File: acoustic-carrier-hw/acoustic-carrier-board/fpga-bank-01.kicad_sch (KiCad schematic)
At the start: 8 parts, among them IC1 ECP5-BGA256

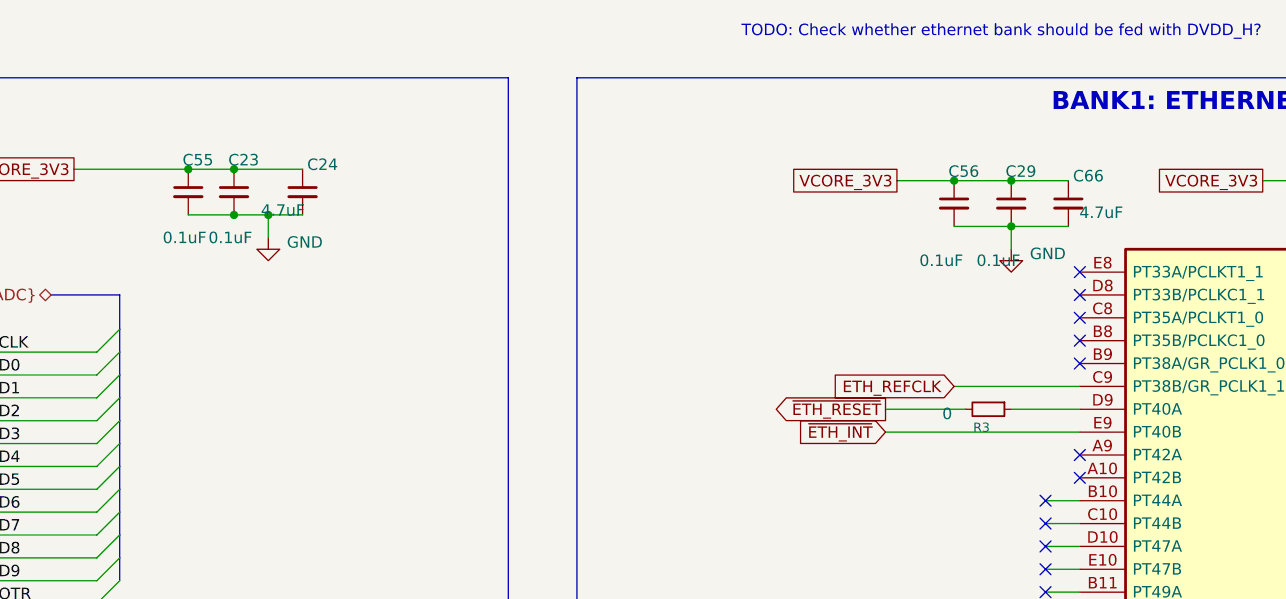
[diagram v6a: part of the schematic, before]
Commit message: [carrier] Finished rough layout, p (put together according to component category
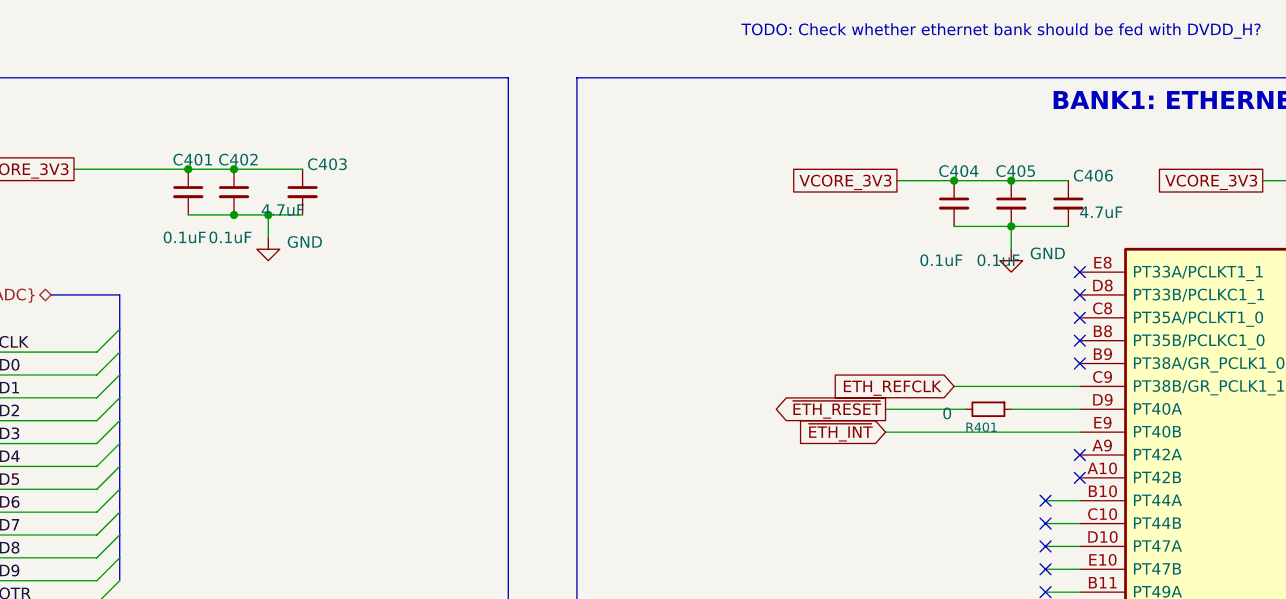
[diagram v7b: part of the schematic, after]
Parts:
- renumbered C55 to C401, C23 to C402, C24 to C403, C56 to C404, C29 to C405, C66 to C406, R3 to R401
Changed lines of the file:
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@@
 		(on_board yes)
 		(dnp no)
-		(property "Reference" "C55"
+		(property "Reference" "C401"
 			(at 115.824 45.974 0)
 			(effects
@@
 			(project "acoustic-carrier-board"
 				(path "/25b015c9-ab13-4427-b72c-b6f348597100/7e06bbd5-1e52-404d-be87-b09140719274"
-					(reference "C55")
+					(reference "C401")
 					(unit 1)
 				)
@@
 		(on_board yes)
 		(dnp no)
-		(property "Reference" "C66"
+		(property "Reference" "C406"
 			(at 211.328 47.752 0)
 			(effects
@@
 			(project "acoustic-carrier-board"
 				(path "/25b015c9-ab13-4427-b72c-b6f348597100/7e06bbd5-1e52-404d-be87-b09140719274"
-					(reference "C66")
+					(reference "C406")
 					(unit 1)
 				)
@@
 		(on_board yes)
 		(dnp no)
-		(property "Reference" "#PWR014"
+		(property "Reference" "#PWR0401"
 			(at 121.92 60.96 0)
 			(effects
@@
 			(project "acoustic-carrier-board"
 				(path "/25b015c9-ab13-4427-b72c-b6f348597100/7e06bbd5-1e52-404d-be87-b09140719274"
-					(reference "#PWR014")
+					(reference "#PWR0401")
 					(unit 1)
 				)
@@
 		(on_board yes)
 		(dnp no)
-		(property "Reference" "#PWR08"
+		(property "Reference" "#PWR0402"
 			(at 204.47 62.23 0)
 			(effects
@@
 			(project "acoustic-carrier-board"
 				(path "/25b015c9-ab13-4427-b72c-b6f348597100/7e06bbd5-1e52-404d-be87-b09140719274"
-					(reference "#PWR08")
+					(reference "#PWR0402")
 					(unit 1)
 				)
@@
 		(on_board yes)
 		(dnp no)
-		(property "Reference" "C56"
+		(property "Reference" "C404"
 			(at 200.914 47.244 0)
 			(effects
@@
 			(project "acoustic-carrier-board"
 				(path "/25b015c9-ab13-4427-b72c-b6f348597100/7e06bbd5-1e52-404d-be87-b09140719274"
-					(reference "C56")
+					(reference "C404")
 					(unit 1)
 				)
@@
 		(on_board yes)
 		(dnp no)
-		(property "Reference" "C24"
+		(property "Reference" "C403"
 			(at 126.238 46.482 0)
 			(effects
@@
 			(project "acoustic-carrier-board"
 				(path "/25b015c9-ab13-4427-b72c-b6f348597100/7e06bbd5-1e52-404d-be87-b09140719274"
-					(reference "C24")
+					(reference "C403")
 					(unit 1)
 				)
@@
 		(on_board yes)
 		(dnp no)
-		(property "Reference" "C23"
+		(property "Reference" "C402"
 			(at 120.904 45.974 0)
 			(effects
@@
 			(project "acoustic-carrier-board"
 				(path "/25b015c9-ab13-4427-b72c-b6f348597100/7e06bbd5-1e52-404d-be87-b09140719274"
-					(reference "C23")
+					(reference "C402")
 					(unit 1)
 				)
@@
 		(on_board yes)
 		(dnp no)
-		(property "Reference" "C29"
+		(property "Reference" "C405"
 			(at 207.264 47.244 0)
 			(effects
@@
 			(project "acoustic-carrier-board"
 				(path "/25b015c9-ab13-4427-b72c-b6f348597100/7e06bbd5-1e52-404d-be87-b09140719274"
-					(reference "C29")
+					(reference "C405")
 					(unit 1)
 				)
@@
 		(on_board yes)
 		(dnp no)
-		(property "Reference" "R3"
+		(property "Reference" "R401"
 			(at 201.168 75.692 90)
 			(effects
@@
 			(project "acoustic-carrier-board"
 				(path "/25b015c9-ab13-4427-b72c-b6f348597100/7e06bbd5-1e52-404d-be87-b09140719274"
-					(reference "R3")
+					(reference "R401")
 					(unit 1)
 				)

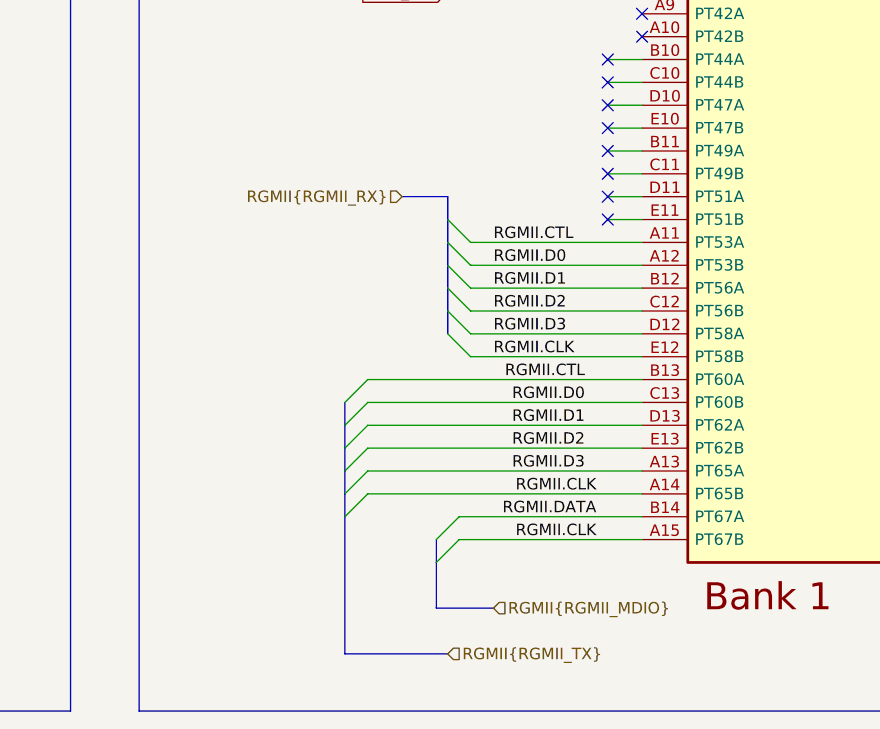
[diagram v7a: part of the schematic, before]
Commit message: [¢arrier] Added netties and determined trace geometry for 50 ohms SE / 100 ohms DIFF impedance (next) reset the appropriate DQS group signals, RGMII and USB signals
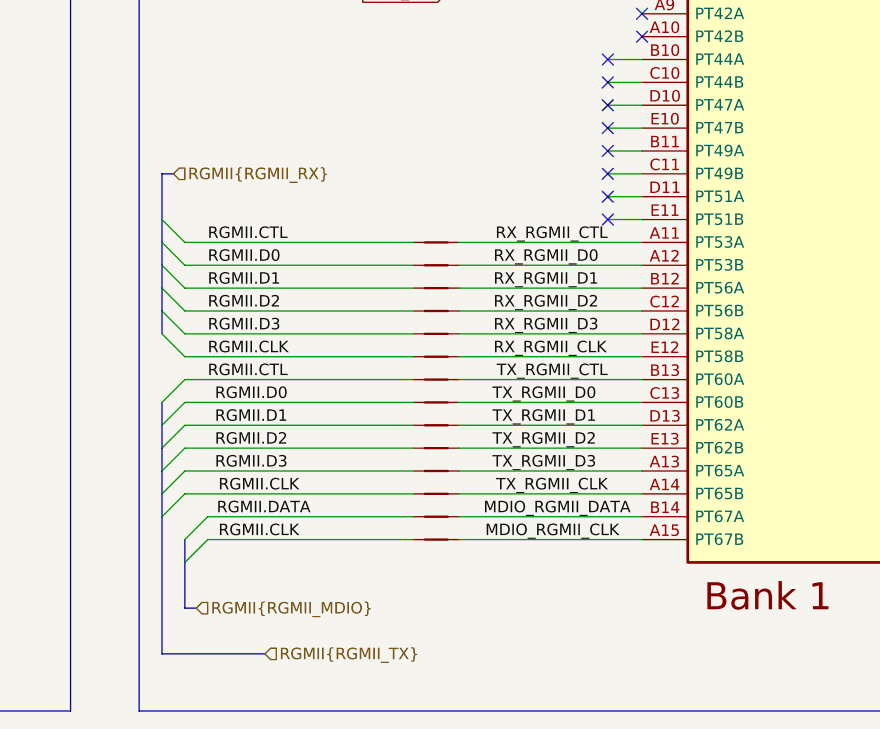
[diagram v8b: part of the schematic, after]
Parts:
- added NT401, NT402, NT403, NT404, NT405, NT406, NT407, NT408, NT409, NT410, NT415, NT416, NT417, NT418: NetTie_2, iw-misc:NetTie-2_SMD_Pad0.1565mm, symbol Device:NetTie_2
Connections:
- net RGMII.CLK: now also NT402.1, NT408.1, NT410.1; no longer IC1.A14 (PT65B), IC1.A15 (PT67B), IC1.E12 (PT58B)
- net RGMII.CTL: now also NT403.1, NT415.1; no longer IC1.A11 (PT53A), IC1.B13 (PT60A)
- net RGMII.D0: now also NT404.1, NT416.1; no longer IC1.A12 (PT53B), IC1.C13 (PT60B)
- net RGMII.D1: now also NT405.1, NT417.1; no longer IC1.B12 (PT56A), IC1.D13 (PT62A)
- net RGMII.D2: now also NT406.1, NT418.1; no longer IC1.C12 (PT56B), IC1.E13 (PT62B)
- net RGMII.D3: now also NT401.1, NT407.1; no longer IC1.A13 (PT65A), IC1.D12 (PT58A)
- net RGMII.DATA: now also NT409.1; no longer IC1.B14 (PT67A)
- new net MDIO_RGMII_CLK: IC1.A15 (PT67B), NT410.2
- new net MDIO_RGMII_DATA: IC1.B14 (PT67A), NT409.2
- new net RX_RGMII_CLK: IC1.E12 (PT58B), NT402.2
- new net RX_RGMII_CTL: IC1.A11 (PT53A), NT415.2
- new net RX_RGMII_D0: IC1.A12 (PT53B), NT416.2
- new net RX_RGMII_D1: IC1.B12 (PT56A), NT417.2
- new net RX_RGMII_D2: IC1.C12 (PT56B), NT418.2
- new net RX_RGMII_D3: IC1.D12 (PT58A), NT401.2
- new net TX_RGMII_CLK: IC1.A14 (PT65B), NT408.2
- new net TX_RGMII_CTL: IC1.B13 (PT60A), NT403.2
- new net TX_RGMII_D0: IC1.C13 (PT60B), NT404.2
- new net TX_RGMII_D1: IC1.D13 (PT62A), NT405.2
- new net TX_RGMII_D2: IC1.E13 (PT62B), NT406.2
- new net TX_RGMII_D3: IC1.A13 (PT65A), NT407.2
